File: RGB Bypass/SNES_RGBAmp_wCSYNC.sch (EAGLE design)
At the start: 31 parts, among them J3 SNES_MULTIAV_RGBC_ONLY, U1 THS7374

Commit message: go to version 4.1
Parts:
- R41: value 8k66 -> 9k53
- R42: value 1k4 -> 620
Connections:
- removed net N$12: R13.2, U1G$1.CO1
- removed net N$13: R23.2, U1G$1.CO2
- new net N$11: R33.2, U1G$1.CO4
- new net N$7: R23.2, U1G$1.CO3
- net N$1: now also U1G$1.CI2; no longer U1G$1.CI1
- net N$10: now also U1G$1.CI1; no longer U1G$1.CI4
- net N$18: now also U1G$1.CO1; no longer U1G$1.CO4
- net N$2: now also U1G$1.CI3; no longer U1G$1.CI2
- net N$8: now also R13.2, U1G$1.CO2; no longer R33.2, U1G$1.CO3
- net R9: now also U1G$1.CI4; no longer U1G$1.CI3
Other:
- moved on the sheet: B, C11, C21, C31, C43, CS, G, J2, R, R13, R23, R33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

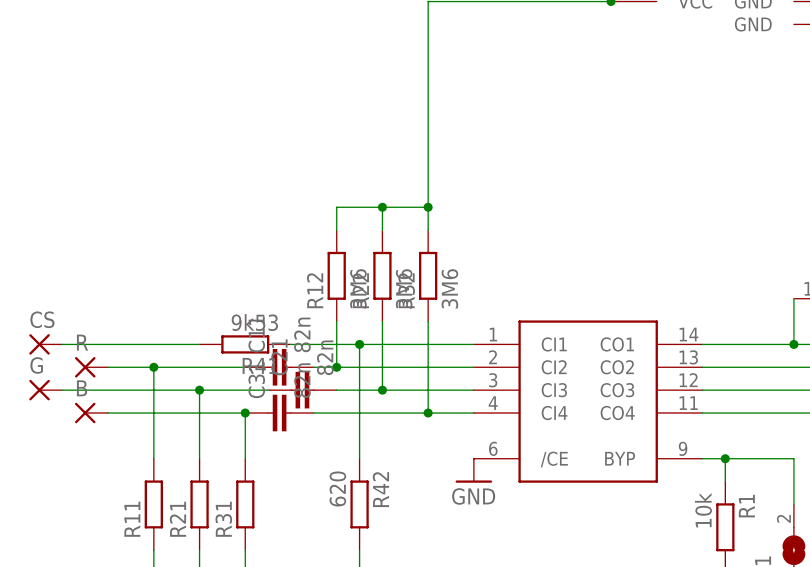
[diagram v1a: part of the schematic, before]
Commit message: Change resistor values
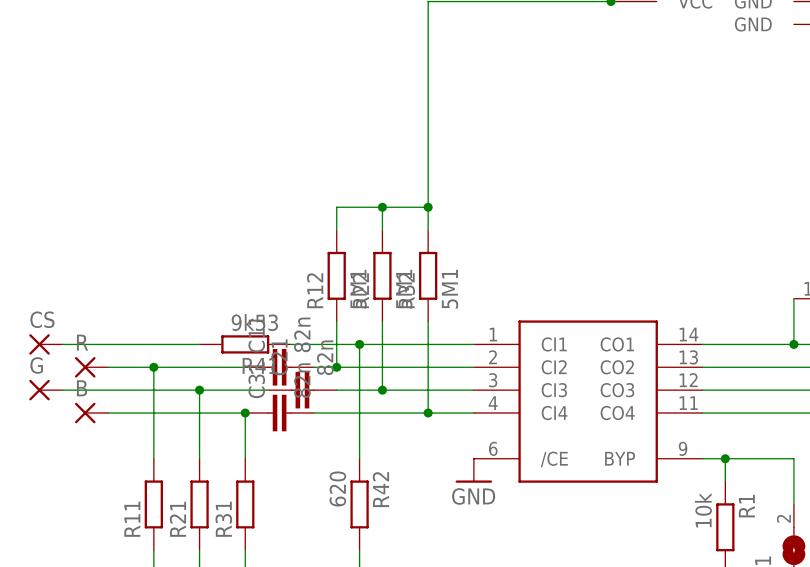
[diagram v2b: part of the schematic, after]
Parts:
- R12, R22, R32: value 3M6 -> 5M1
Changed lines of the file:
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@@
 <part name="R21" library="rcl" deviceset="R-EU_" device="R0603"/>
 <part name="R31" library="rcl" deviceset="R-EU_" device="R0603"/>
-<part name="R12" library="rcl" deviceset="R-EU_" device="R0603" value="3M6"/>
-<part name="R22" library="rcl" deviceset="R-EU_" device="R0603" value="3M6"/>
-<part name="R32" library="rcl" deviceset="R-EU_" device="R0603" value="3M6"/>
+<part name="R12" library="rcl" deviceset="R-EU_" device="R0603" value="5M1"/>
+<part name="R22" library="rcl" deviceset="R-EU_" device="R0603" value="5M1"/>
+<part name="R32" library="rcl" deviceset="R-EU_" device="R0603" value="5M1"/>
 <part name="R13" library="rcl" deviceset="R-EU_" device="R0603"/>
 <part name="R23" library="rcl" deviceset="R-EU_" device="R0603"/>
